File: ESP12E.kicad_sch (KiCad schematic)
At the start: 32 parts, among them J1 Conn_01x06_Pin, J2 Conn_01x06_Pin, P1 USB_C_Plug_USB2.0, Q3 SS8050, Q4 SS8050, U1 ESP-12E, U2 CH340G, U3 AMS1117-3.3, Y1 Crystal_GND23

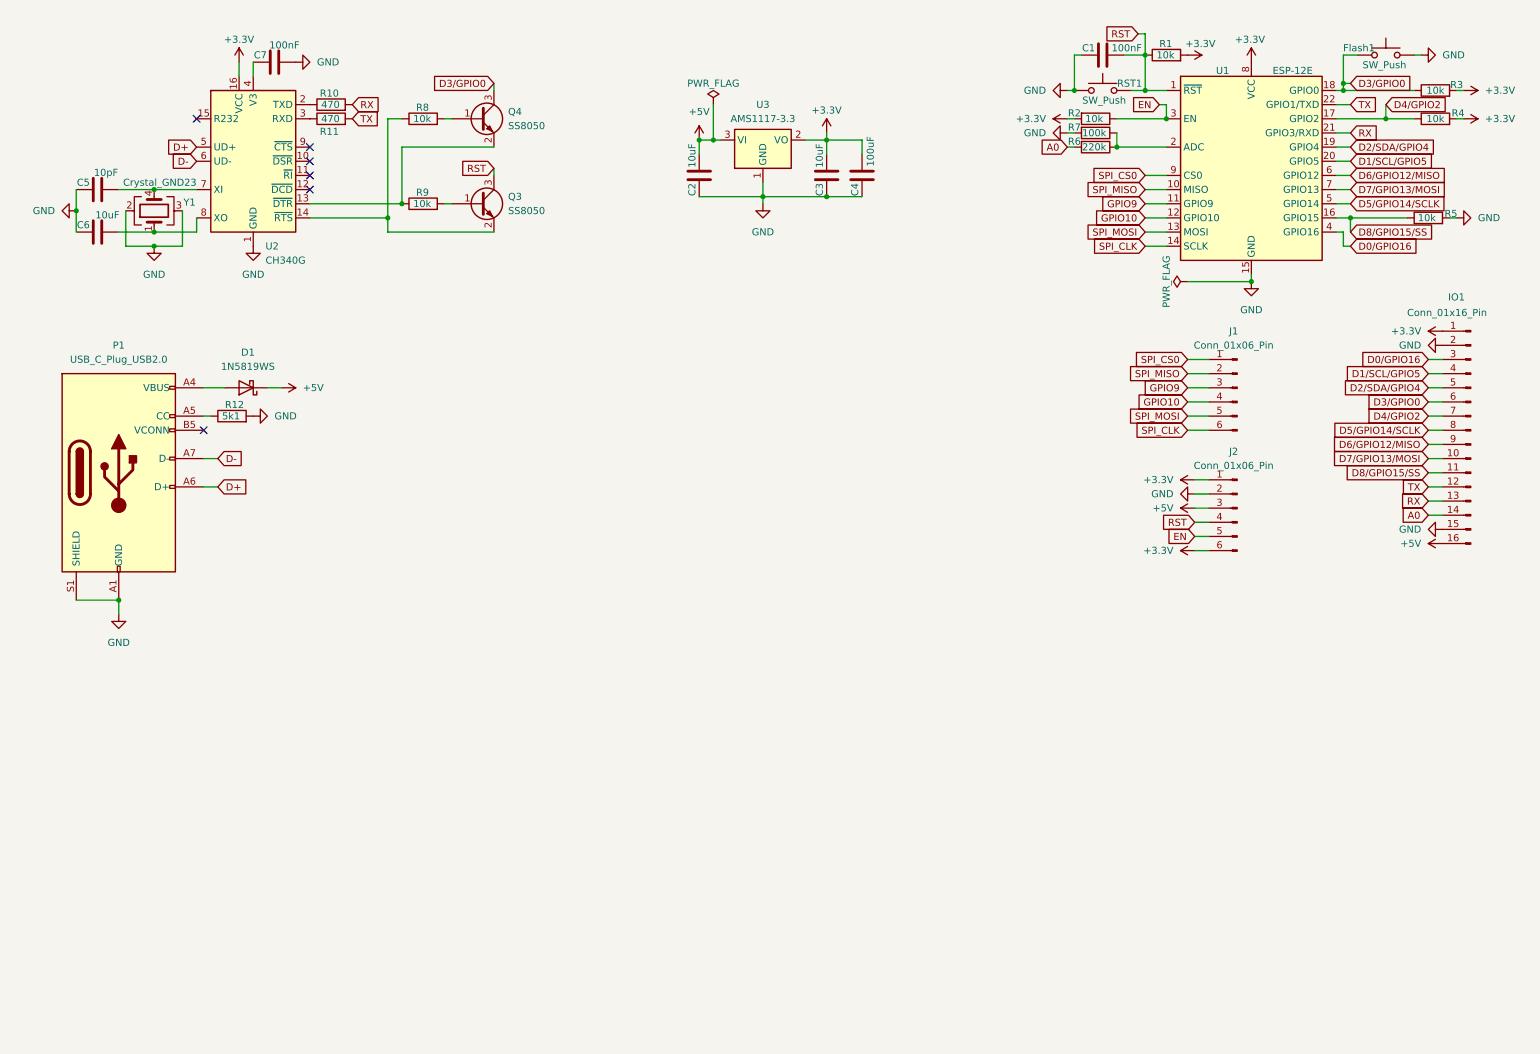
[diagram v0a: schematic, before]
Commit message: Feat: adding IRF520 mosfets for controlling Motor of air pump and 4 solinoids.
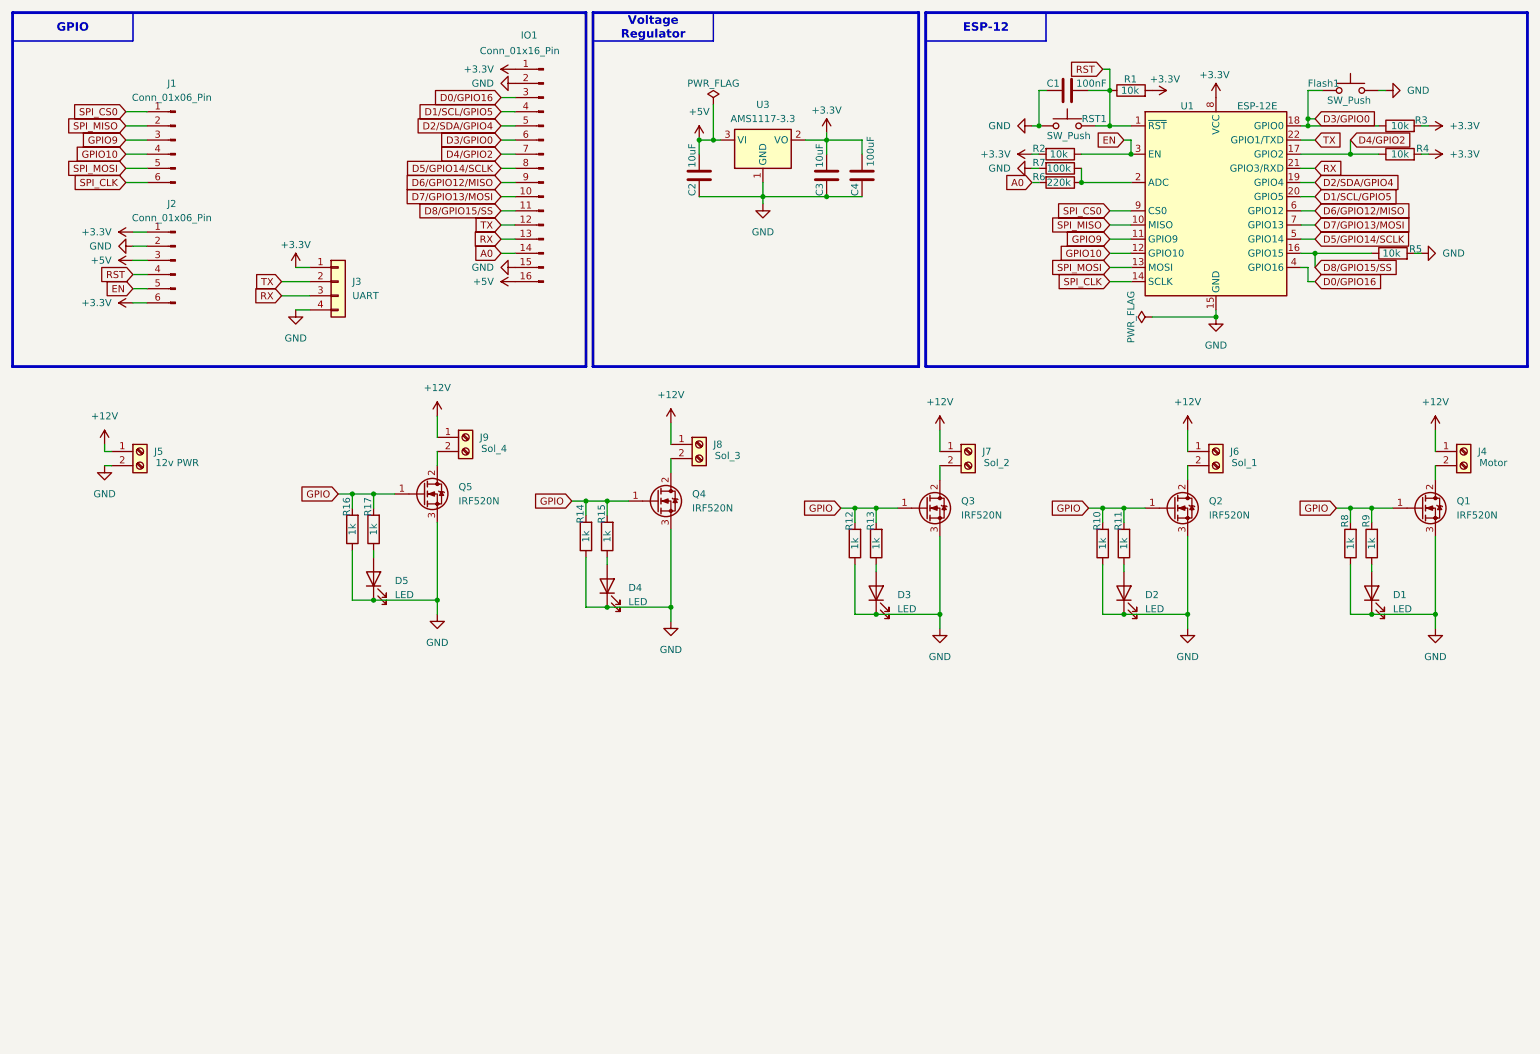
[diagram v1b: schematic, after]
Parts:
- removed C5: 10pF, Capacitor_SMD:C_0201_0603Metric, symbol Device:C
- removed C6: 10uF, Capacitor_SMD:C_0201_0603Metric, symbol Device:C
- removed C7: 100nF, Capacitor_SMD:C_0201_0603Metric, symbol Device:C
- removed D1: 1N5819WS, Diode_SMD:D_SOD-323, symbol Diode:1N5819WS
- removed P1: USB_C_Plug_USB2.0, Connector_USB:USB_C_Receptacle_GCT_USB4125-xx-x_6P_TopMnt_Horizontal, symbol Connector:USB_C_Plug_USB2.0
- removed Q3, Q4: SS8050, Package_TO_SOT_SMD:SOT-23, symbol Transistor_BJT:SS8050
- removed U2: CH340G, Package_SO:SOIC-16_3.9x9.9mm_P1.27mm, symbol Interface_USB:CH340G
- removed Y1: Crystal_GND23, Crystal:Crystal_SMD_3225-4Pin_3.2x2.5mm, symbol Device:Crystal_GND23
- added D1, D2, D3, D4, D5: LED, LED_SMD:LED_1206_3216Metric, symbol Device:LED
- added J3: UART, Connector_JST:JST_XH_B4B-XH-A_1x04_P2.50mm_Vertical, symbol Connector_Generic:Conn_01x04
- added J4: Motor, TerminalBlock_Phoenix:TerminalBlock_Phoenix_PT-1,5-2-5.0-H_1x02_P5.00mm_Horizontal, symbol Connector:Screw_Terminal_01x02
- added J5: 12v PWR, TerminalBlock_Phoenix:TerminalBlock_Phoenix_PT-1,5-2-5.0-H_1x02_P5.00mm_Horizontal, symbol Connector:Screw_Terminal_01x02
- added J6: Sol_1, TerminalBlock_Phoenix:TerminalBlock_Phoenix_PT-1,5-2-5.0-H_1x02_P5.00mm_Horizontal, symbol Connector:Screw_Terminal_01x02
- added J7: Sol_2, TerminalBlock_Phoenix:TerminalBlock_Phoenix_PT-1,5-2-5.0-H_1x02_P5.00mm_Horizontal, symbol Connector:Screw_Terminal_01x02
- added J8: Sol_3, TerminalBlock_Phoenix:TerminalBlock_Phoenix_PT-1,5-2-5.0-H_1x02_P5.00mm_Horizontal, symbol Connector:Screw_Terminal_01x02
- added J9: Sol_4, TerminalBlock_Phoenix:TerminalBlock_Phoenix_PT-1,5-2-5.0-H_1x02_P5.00mm_Horizontal, symbol Connector:Screw_Terminal_01x02
- added Q1, Q2, Q3, Q4, Q5: IRF520N, Package_TO_SOT_THT:TO-220-3_Vertical, symbol Transistor_FET:IRF540N
- added R13, R14, R15, R16, R17: 1k, Resistor_THT:R_Axial_DIN0309_L9.0mm_D3.2mm_P12.70mm_Horizontal, symbol Device:R
- C1, C4: footprint Capacitor_SMD:C_0201_0603Metric -> Capacitor_THT:C_Disc_D3.0mm_W2.0mm_P2.50mm
- C2, C3: footprint Capacitor_SMD:C_0201_0603Metric -> Capacitor_THT:C_Radial_D5.0mm_H5.0mm_P2.00mm
- R1: footprint Resistor_SMD:R_0201_0603Metric -> Resistor_THT:R_Axial_DIN0309_L9.0mm_D3.2mm_P12.70mm_Horizontal
- R10, R11: value 470 -> 1k; footprint Resistor_SMD:R_0201_0603Metric -> Resistor_THT:R_Axial_DIN0309_L9.0mm_D3.2mm_P12.70mm_Horizontal
- R12: value 5k1 -> 1k; footprint Resistor_SMD:R_0201_0603Metric -> Resistor_THT:R_Axial_DIN0309_L9.0mm_D3.2mm_P12.70mm_Horizontal
- R2, R3, R4, R5, R6, R7: footprint Resistor_SMD:R_0402_1005Metric -> Resistor_THT:R_Axial_DIN0309_L9.0mm_D3.2mm_P12.70mm_Horizontal
- R8, R9: value 10k -> 1k; footprint Resistor_SMD:R_0201_0603Metric -> Resistor_THT:R_Axial_DIN0309_L9.0mm_D3.2mm_P12.70mm_Horizontal
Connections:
- net +3.3V: now also J3.1 (Pin_1)
- net GND: now also R10.1, R12.1, R8.1, D1.1 (K), D2.1 (K), D3.1 (K), D4.1 (K), D5.1 (K), J3.4 (Pin_4), J5.2 (Pin_2), Q1.3 (S), Q2.3 (S), Q3.3 (S), Q4.3 (S), Q5.3 (S), R14.1, R16.1; no longer R12.2
- net RX: now also J3.3 (Pin_3); no longer R10.2
- net TX: now also J3.2 (Pin_2); no longer R11.2
- net at R9.1: now also D1.2 (A)
- net GPIO: now reaches R9.2
- net GPIO: now also R10.2, R11.2, R12.2, R8.2, Q1.1 (G), Q2.1 (G), Q3.1 (G), Q4.1 (G), Q5.1 (G), R13.2, R14.2, R15.2, R16.2, R17.2
- net at R11.1: now also D2.2 (A)
- new net: J7.2 (Pin_2), Q3.2 (D)
- new net: J4.2 (Pin_2), Q1.2 (D)
- new net: J9.2 (Pin_2), Q5.2 (D)
- new net: D4.2 (A), R15.1
- new net: J8.2 (Pin_2), Q4.2 (D)
- new net: D5.2 (A), R17.1
- new net: J6.2 (Pin_2), Q2.2 (D)
- new net: D3.2 (A), R13.1
- new net +12V: J4.1 (Pin_1), J5.1 (Pin_1), J6.1 (Pin_1), J7.1 (Pin_1), J8.1 (Pin_1), J9.1 (Pin_1)
- no-connect marks 6 -> 0
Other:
- company: (none) -> Metanoia
- title: (none) -> ESP-12 Circuit for Pressure control
- moved on the sheet: C1, Flash1, IO1, J1, J2, R1, R2, R3, R4, R5, R6, R7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

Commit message: feat: pcb is ok now, next Pressure sensor.
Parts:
- added U2: LM7805_TO220, Package_TO_SOT_THT:TO-220-3_Vertical, symbol Regulator_Linear:LM7805_TO220
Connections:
- net +12V: now also U2.1 (VI)
- net +5V: now also U2.3 (VO)
- net D1/SCL/GPIO5: now also Q5.1 (G), R16.2, R17.2
- net D2/SDA/GPIO4: now also Q4.1 (G), R14.2, R15.2
- net D5/GPIO14/SCLK: now also Q1.1 (G), R8.2, R9.2
- net D6/GPIO12/MISO: now also Q2.1 (G), R10.2, R11.2
- net D7/GPIO13/MOSI: now also Q3.1 (G), R12.2, R13.2
- net GND: now also U2.2 (GND)
- net RX: now also J3.2 (Pin_2); no longer J3.3 (Pin_3)
- net TX: now also J3.3 (Pin_3); no longer J3.2 (Pin_2)
- removed net GPIO: Q1.1 (G), Q2.1 (G), Q3.1 (G), Q4.1 (G), Q5.1 (G), R10.2, R11.2, R12.2, R13.2, R14.2, R15.2, R16.2, R17.2, R8.2, R9.2
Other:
- moved on the sheet: C2, C3, C4, U3

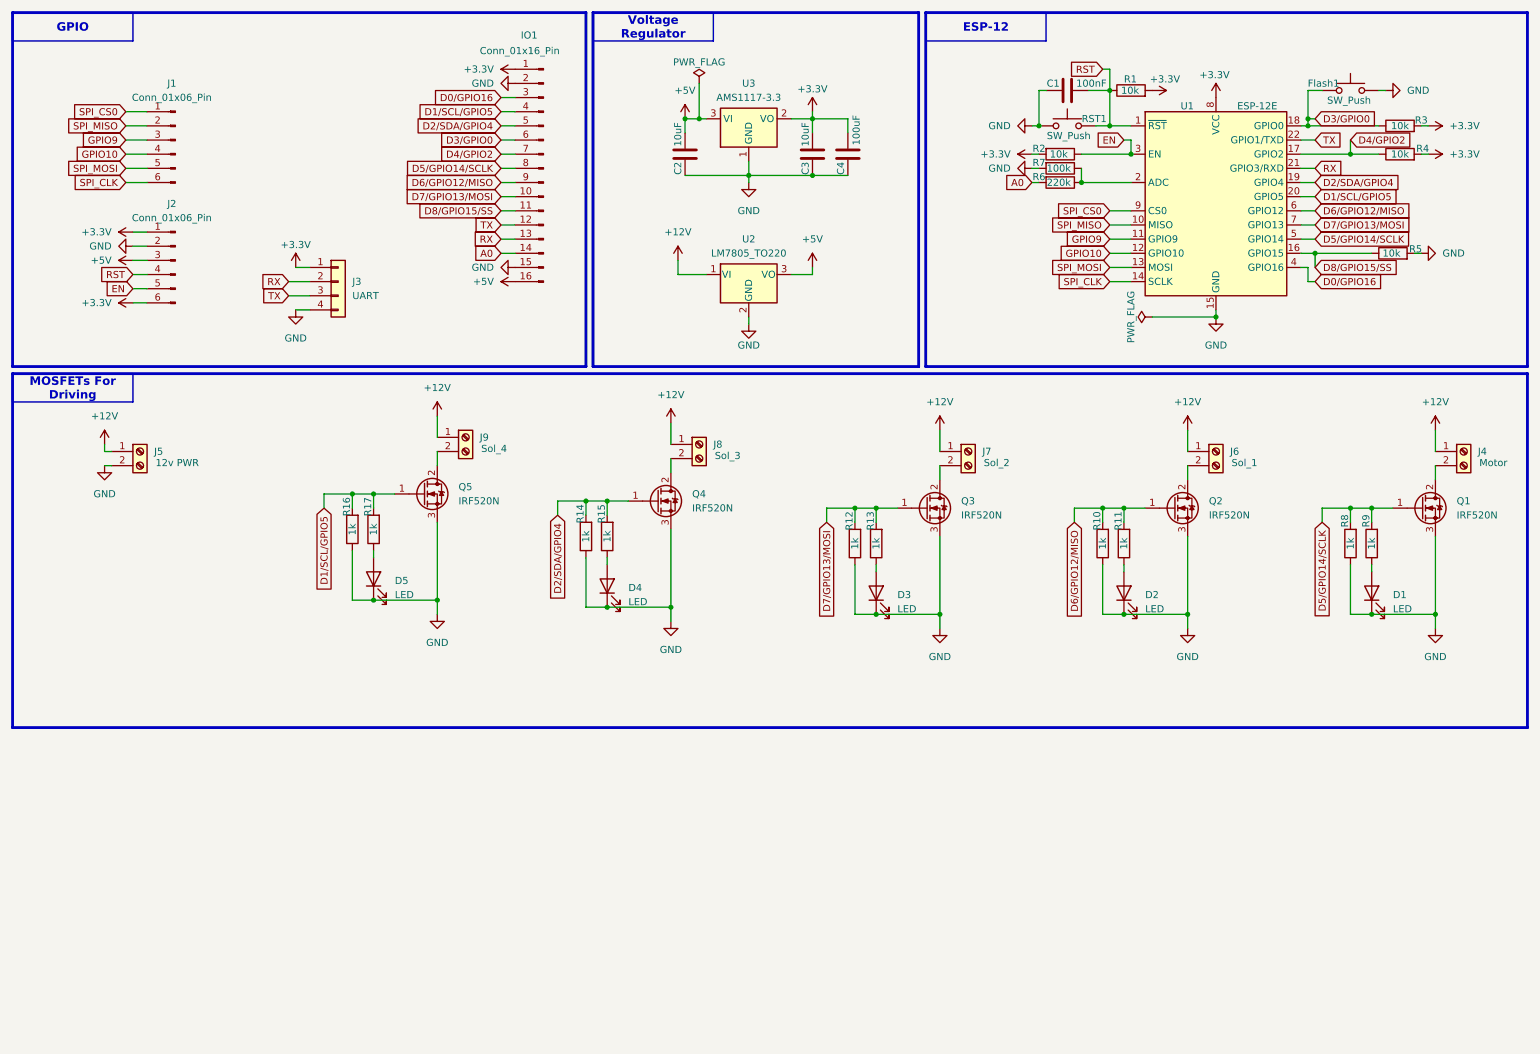
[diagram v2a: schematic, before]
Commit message: Working: on adding air pressure sensors (MPS-2108).
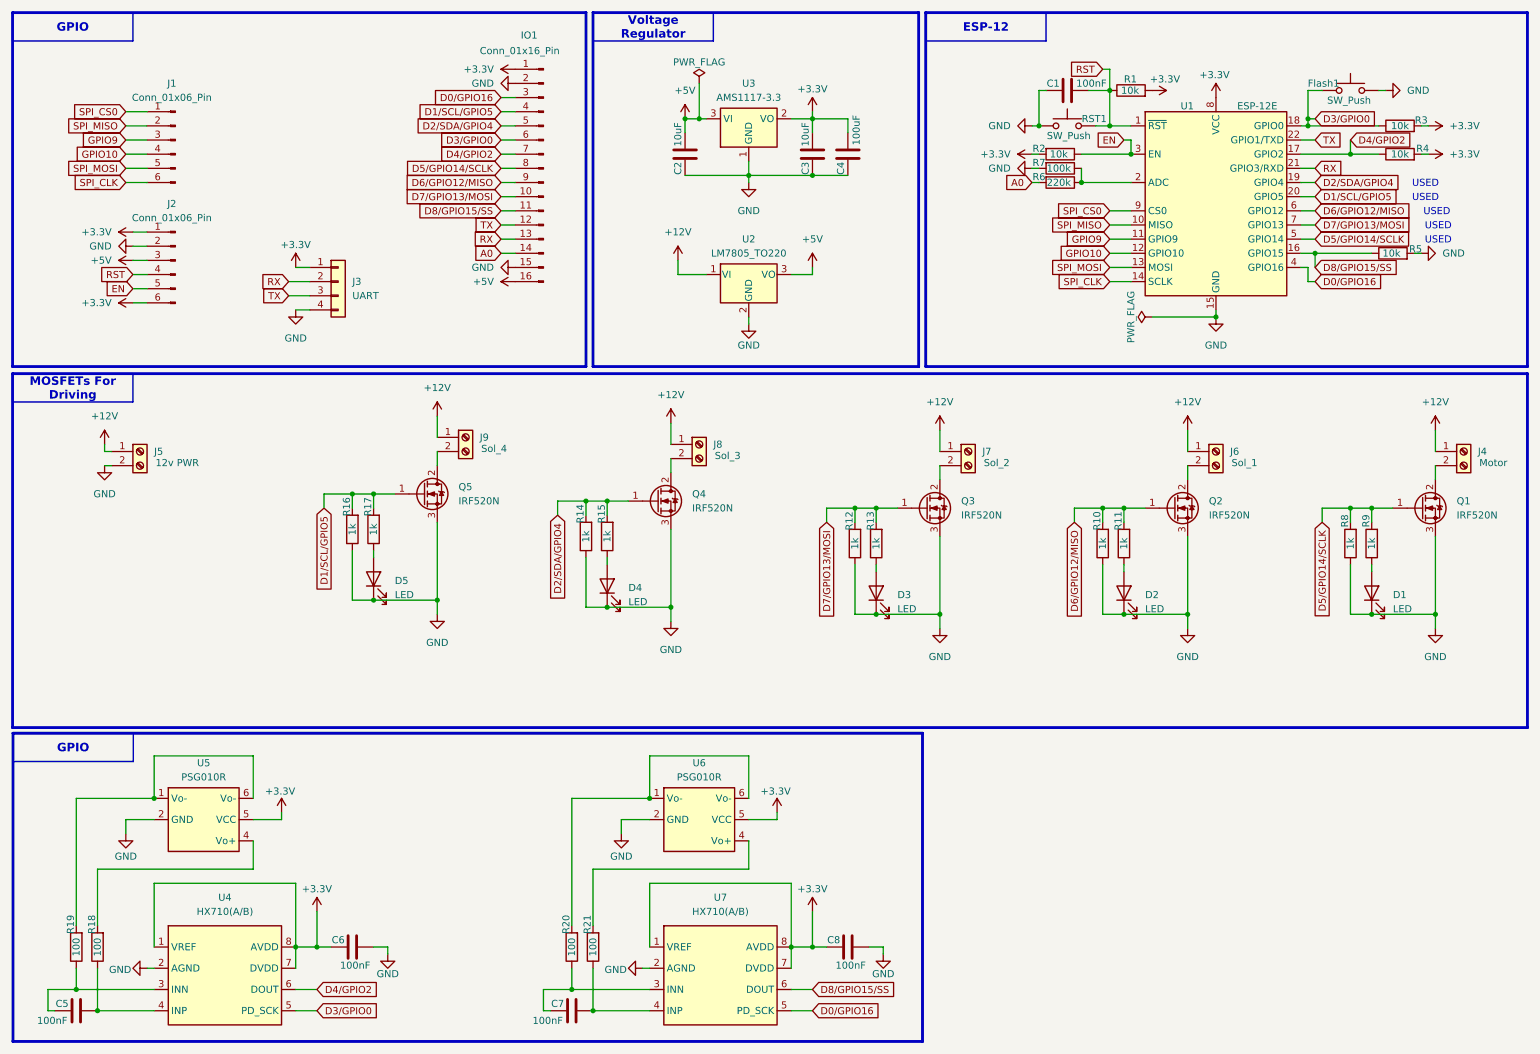
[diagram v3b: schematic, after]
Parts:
- added C5, C6, C7, C8: 100nF, Capacitor_THT:C_Disc_D3.0mm_W2.0mm_P2.50mm, symbol Device:C
- added R18, R19, R20, R21: 100, Resistor_THT:R_Axial_DIN0309_L9.0mm_D3.2mm_P12.70mm_Horizontal, symbol Device:R
- added U4, U7: HX710(A/B), Package_SO:SOP-8_3.9x4.9mm_P1.27mm, symbol Analog_ADC:HX710(A/B)
- added U5, U6: PSG010R, Package_DIP:DIP-6_W10.16mm, symbol Sensor_Pressure:PSG010R
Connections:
- net +3.3V: now also C6.1, C8.1, U4.1 (VREF), U4.7 (DVDD), U4.8 (AVDD), U5.5 (VCC), U6.5 (VCC), U7.1 (VREF), U7.7 (DVDD), U7.8 (AVDD)
- net D0/GPIO16: now also U7.5 (PD_SCK)
- net D3/GPIO0: now also U4.5 (PD_SCK)
- net D4/GPIO2: now also U4.6 (DOUT)
- net D8/GPIO15/SS: now also U7.6 (DOUT)
- net GND: now also C6.2, C8.2, U4.2 (AGND), U5.2 (GND), U6.2 (GND), U7.2 (AGND)
- new net: C5.1, R19.1, U4.3 (INN)
- new net: R19.2, U5.1 (Vo-), U5.6 (Vo-)
- new net: C5.2, R18.1, U4.4 (INP)
- new net: R20.2, U6.1 (Vo-), U6.6 (Vo-)
- new net: R21.2, U6.4 (Vo+)
- new net: R18.2, U5.4 (Vo+)
- new net: C7.1, R20.1, U7.3 (INN)
- new net: C7.2, R21.1, U7.4 (INP)
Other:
- note added: "USED"
